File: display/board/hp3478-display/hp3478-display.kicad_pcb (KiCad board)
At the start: 2 copper layers, 130.2 x 29.8 mm, 257 parts, among them J1 SFV10R-1ST, J2 DNP, U1 PIC16F15274-I/MP, U2 DNP

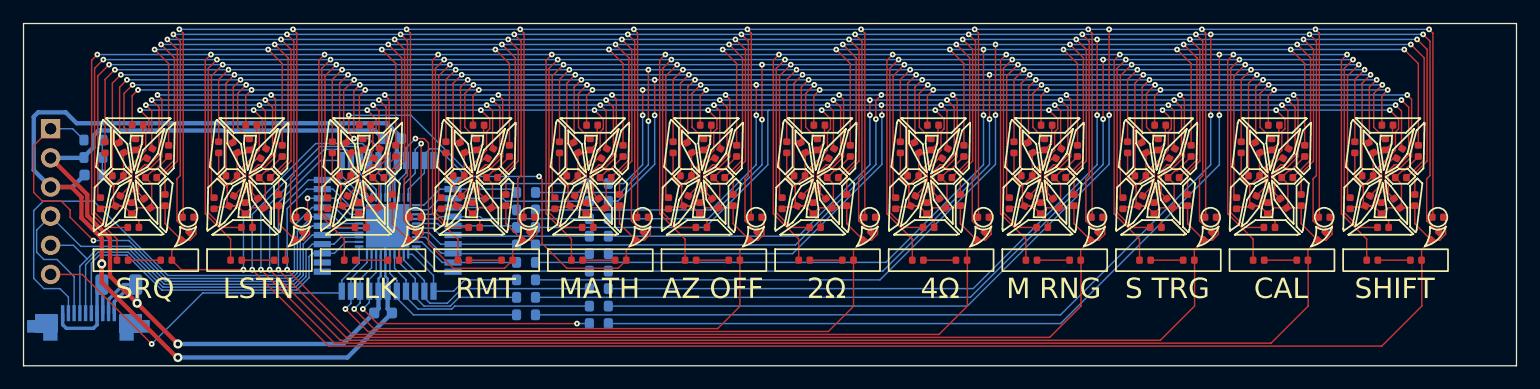
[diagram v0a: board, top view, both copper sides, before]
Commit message: Add mounting holes and fiducials.
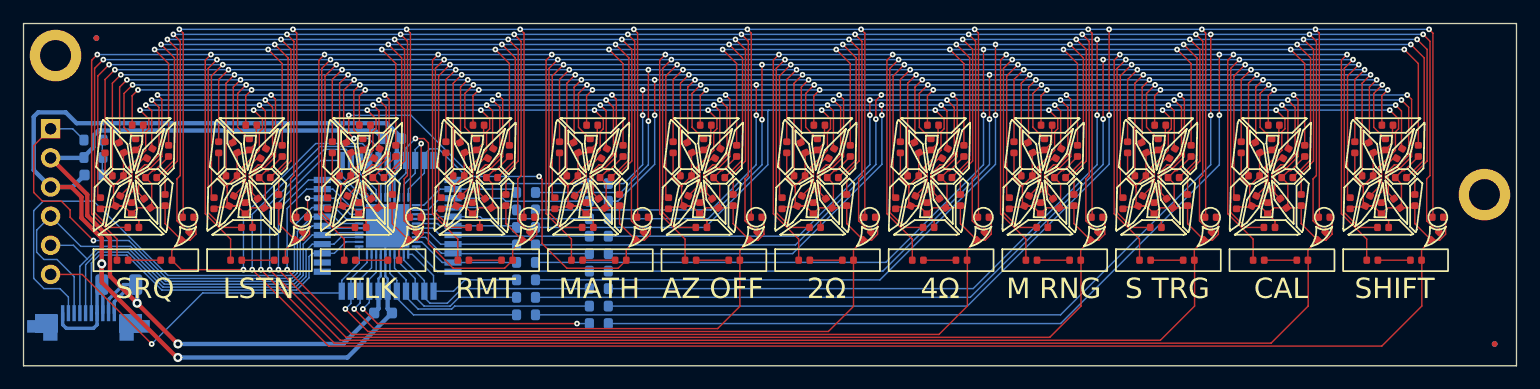
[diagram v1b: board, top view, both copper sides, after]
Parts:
- added FD1: Fiducial_0.5mm_Mask1.5mm, Fiducial:Fiducial_0.5mm_Mask1.5mm, F.Cu at (82.5, 52.1)
- added FD2: Fiducial_0.5mm_Mask1.5mm, Fiducial:Fiducial_0.5mm_Mask1.5mm, F.Cu at (204.5, 78.7)
- added FD3: Fiducial_0.5mm_Mask1.5mm, Fiducial:Fiducial_0.5mm_Mask1.5mm, B.Cu at (82.5, 52.1)
- added FD4: Fiducial_0.5mm_Mask1.5mm, Fiducial:Fiducial_0.5mm_Mask1.5mm, B.Cu at (204.5, 78.7)
- added MH1: MountingHole_2.7mm_M2.5_ISO14580_Pad, MountingHole:MountingHole_2.7mm_M2.5_ISO14580_Pad, F.Cu at (79.0, 53.6)
- added MH2: MountingHole_2.7mm_M2.5_ISO14580_Pad, MountingHole:MountingHole_2.7mm_M2.5_ISO14580_Pad, F.Cu at (203.6, 65.7)
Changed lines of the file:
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@@
     )
   )
+  (footprint "Fiducial:Fiducial_0.5mm_Mask1.5mm" (layer "F.Cu")
+    (at 204.47 78.74)
+    (descr "Circular Fiducial, 0.5mm bare copper, 1.5mm soldermask opening")
+    (tags "fiducial")
+    (attr smd board_only exclude_from_bom)
+    (fp_text reference "FD2" (at 0 -1.7145) (layer "F.SilkS") hide
+      (effects (font (size 1 1) (thickness 0.15)))
+    )
+    (fp_text value "Fiducial_0.5mm_Mask1.5mm" (at 0 1.7145) (layer "F.Fab") hide
+      (effects (font (size 1 1) (thickness 0.15)))
+    )
+    (fp_text user "${REFERENCE}" (at 0 0) (layer "F.Fab") hide
+      (effects (font (size 0.2 0.2) (thickness 0.04)))
+    )
+    (fp_circle (center 0 0) (end 1 0) (layer "F.CrtYd") (width 0.05) (fill none))
+    (fp_circle (center 0 0) (end 0.75 0) (layer "F.Fab") (width 0.1) (fill none))
+    (pad "" smd circle (at 0 0) (size 0.5 0.5) (layers "F.Cu" "F.Mask")
+      (solder_mask_margin 0.5) (clearance 0.5))
+  )
   (footprint "0Local:LED_0402_1005Metric" (layer "F.Cu")
     (at 94.3356 64.0842 180)
@@
     )
   )
+  (footprint "Fiducial:Fiducial_0.5mm_Mask1.5mm" (layer "F.Cu")
+    (at 82.55 52.07)
+    (descr "Circular Fiducial, 0.5mm bare copper, 1.5mm soldermask opening")
+    (tags "fiducial")
+    (attr smd board_only exclude_from_bom)
+    (fp_text reference "FD1" (at 0 -1.7145) (layer "F.SilkS") hide
+      (effects (font (size 1 1) (thickness 0.15)))
+    )
+    (fp_text value "Fiducial_0.5mm_Mask1.5mm" (at 0 1.7145) (layer "F.Fab") hide
+      (effects (font (size 1 1) (thickness 0.15)))
+    )
+    (fp_text user "${REFERENCE}" (at 0 0) (layer "F.Fab") hide
+      (effects (font (size 0.2 0.2) (thickness 0.04)))
+    )
+    (fp_circle (center 0 0) (end 1 0) (layer "F.CrtYd") (width 0.05) (fill none))
+    (fp_circle (center 0 0) (end 0.75 0) (layer "F.Fab") (width 0.1) (fill none))
+    (pad "" smd circle (at 0 0) (size 0.5 0.5) (layers "F.Cu" "F.Mask")
+      (solder_mask_margin 0.5) (clearance 0.5))
+  )
   (footprint "0Local:LED_0402_1005Metric" (layer "F.Cu")
     (at 183.4896 64.0842 180)
@@
     )
   )
+  (footprint "MountingHole:MountingHole_2.7mm_M2.5_ISO14580_Pad" (layer "F.Cu")
+    (at 203.581 65.7225)
+    (descr "Mounting Hole 2.7mm, M2.5, ISO14580")
+    (tags "mounting hole 2.7mm m2.5 iso14580")
+    (attr board_only exclude_from_pos_files exclude_from_bom)
+    (fp_text reference "MH2" (at 0 -3.25) (layer "F.SilkS") hide
+      (effects (font (size 1 1) (thickness 0.15)))
+    )
+    (fp_text value "MountingHole_2.7mm_M2.5_ISO14580_Pad" (at 0 3.25) (layer "F.Fab") hide
+      (effects (font (size 1 1) (thickness 0.15)))
+    )
+    (fp_text user "${REFERENCE}" (at 0 0) (layer "F.Fab") hide
+      (effects (font (size 1 1) (thickness 0.15)))
+    )
+    (fp_circle (center 0 0) (end 2.25 0) (layer "Cmts.User") (width 0.15) (fill none))
+    (fp_circle (center 0 0) (end 2.5 0) (layer "F.CrtYd") (width 0.05) (fill none))
+    (pad "1" thru_hole circle (at 0 0) (size 4.5 4.5) (drill 2.7) (layers *.Cu *.Mask))
+  )
   (footprint "0Local:LED_0402_1005Metric" (layer "F.Cu")
     (at 155.4988 59.6646 180)
@@
     )
   )
+  (footprint "MountingHole:MountingHole_2.7mm_M2.5_ISO14580_Pad" (layer "F.Cu")
+    (at 78.994 53.594)
+    (descr "Mounting Hole 2.7mm, M2.5, ISO14580")
+    (tags "mounting hole 2.7mm m2.5 iso14580")
+    (attr board_only exclude_from_pos_files exclude_from_bom)
+    (fp_text reference "MH1" (at 0 -3.25) (layer "F.SilkS") hide
+      (effects (font (size 1 1) (thickness 0.15)))
+    )
+    (fp_text value "MountingHole_2.7mm_M2.5_ISO14580_Pad" (at 0 3.25) (layer "F.Fab") hide
+      (effects (font (size 1 1) (thickness 0.15)))
+    )
+    (fp_text user "${REFERENCE}" (at 0 0) (layer "F.Fab") hide
+      (effects (font (size 1 1) (thickness 0.15)))
+    )
+    (fp_circle (center 0 0) (end 2.25 0) (layer "Cmts.User") (width 0.15) (fill none))
+    (fp_circle (center 0 0) (end 2.5 0) (layer "F.CrtYd") (width 0.05) (fill none))
+    (pad "1" thru_hole circle (at 0 0) (size 4.5 4.5) (drill 2.7) (layers *.Cu *.Mask))
+  )
   (footprint "0Local:LED_0402_1005Metric" (layer "F.Cu")
     (at 94.3356 66.2686 65)
@@
     )
   )
+  (footprint "Fiducial:Fiducial_0.5mm_Mask1.5mm" (layer "B.Cu")
+    (at 82.55 52.07 180)
+    (descr "Circular Fiducial, 0.5mm bare copper, 1.5mm soldermask opening")
+    (tags "fiducial")
+    (attr smd board_only exclude_from_bom)
+    (fp_text reference "FD3" (at 0 1.7145) (layer "B.SilkS") hide
+      (effects (font (size 1 1) (thickness 0.15)) (justify mirror))
+    )
+    (fp_text value "Fiducial_0.5mm_Mask1.5mm" (at 0 -1.7145) (layer "B.Fab") hide
+      (effects (font (size 1 1) (thickness 0.15)) (justify mirror))
+    )
+    (fp_text user "${REFERENCE}" (at 0 0) (layer "B.Fab") hide
+      (effects (font (size 0.2 0.2) (thickness 0.04)) (justify mirror))
+    )
+    (fp_circle (center 0 0) (end 1 0) (layer "B.CrtYd") (width 0.05) (fill none))
+    (fp_circle (center 0 0) (end 0.75 0) (layer "B.Fab") (width 0.1) (fill none))
+    (pad "" smd circle (at 0 0 180) (size 0.5 0.5) (layers "B.Cu" "B.Mask")
+      (solder_mask_margin 0.5) (clearance 0.5))
+  )
   (footprint "Resistor_SMD:R_0603_1608Metric" (layer "B.Cu")
     (at 120.015 67.056)
@@
     (property "Sheetname" "")
     (attr smd)
-    (fp_text reference "J1" (at -4.191 2.413 unlocked) (layer "B.SilkS")
+    (fp_text reference "J1" (at 3.632 2.573 unlocked) (layer "B.SilkS")
       (effects (font (size 1 1) (thickness 0.15)) (justify mirror))
     )
@@
     )
   )
+  (footprint "Fiducial:Fiducial_0.5mm_Mask1.5mm" (layer "B.Cu")
+    (at 204.47 78.74 180)
+    (descr "Circular Fiducial, 0.5mm bare copper, 1.5mm soldermask opening")
+    (tags "fiducial")
+    (attr smd board_only exclude_from_bom)
+    (fp_text reference "FD4" (at 0 1.7145) (layer "B.SilkS") hide
+      (effects (font (size 1 1) (thickness 0.15)) (justify mirror))
+    )
+    (fp_text value "Fiducial_0.5mm_Mask1.5mm" (at 0 -1.7145) (layer "B.Fab") hide
+      (effects (font (size 1 1) (thickness 0.15)) (justify mirror))
+    )
+    (fp_text user "${REFERENCE}" (at 0 0) (layer "B.Fab") hide
+      (effects (font (size 0.2 0.2) (thickness 0.04)) (justify mirror))
+    )
+    (fp_circle (center 0 0) (end 1 0) (layer "B.CrtYd") (width 0.05) (fill none))
+    (fp_circle (center 0 0) (end 0.75 0) (layer "B.Fab") (width 0.1) (fill none))
+    (pad "" smd circle (at 0 0 180) (size 0.5 0.5) (layers "B.Cu" "B.Mask")
+      (solder_mask_margin 0.5) (clearance 0.5))
+  )
   (footprint "0Local:Symbol_Bonsai_6.7mm" (layer "B.Cu")
     (at 201.58 74.93 180)
@@
     )
   )
-  (gr_rect locked (start 76.2 50.8) (end 206.375 80.645) (layer "Edge.Cuts") (width 0.1) (fill none))
+  (gr_rect (start 76.2 50.8) (end 206.375 80.645) (layer "Edge.Cuts") (width 0.1) (fill none))
   (gr_rect (start 82.296 59.055) (end 200.279 69.215) (layer "User.1") (width 0.15) (fill none))
   (gr_rect (start 82.296 70.485) (end 200.279 72.39) (layer "User.1") (width 0.15) (fill none))

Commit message: Remove MCU and move annunciator LEDs to their own matrix row.
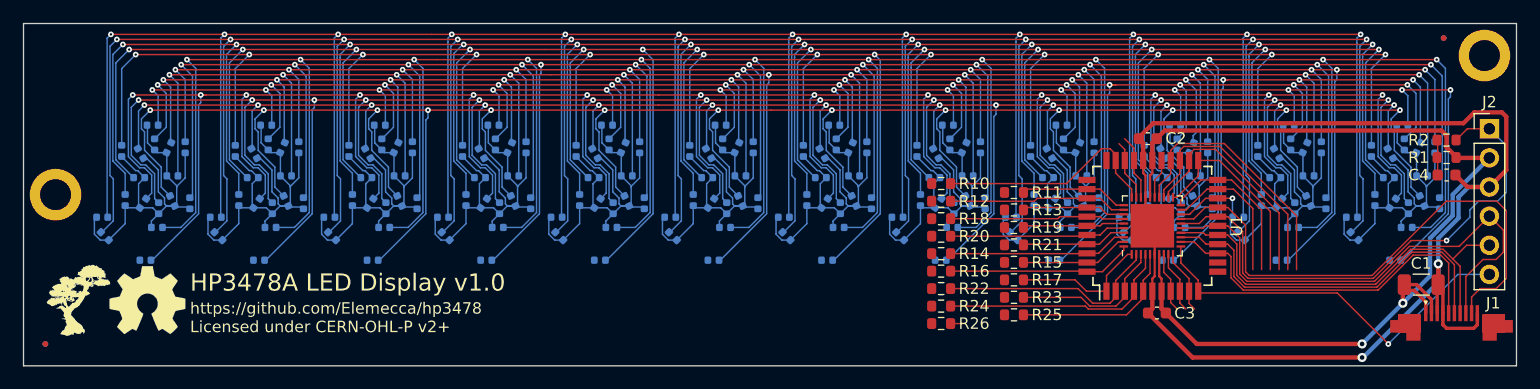
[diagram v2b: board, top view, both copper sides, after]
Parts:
- removed D1018, D1118, D1218, D1318, D218, D318, D418, D518, D618, D718, D818, D918: LED, 0Local:LED_0402_1005Metric
- C1, C2, C3, C4, FD3, FD4, G***, J1, J2, R1, R10, R11, R12, R13, R14, R15, R16, R17, R18, R19, R2, R20, R21, R22, R23, R24, R25, R26, REF**, U1, U2: moved to F.Cu
- D1001, D1002, D1003, D1004, D1005, D1006, D1007, D1008, D1009, D1010, D1011, D1012, D1013, D1014, D1015, D1016, D1101, D1102, D1103, D1104, D1105, D1106, D1107, D1108, D1109, D1110, D1111, D1112, D1113, D1114, D1115, D1116, D1201, D1202, D1203, D1204, D1205, D1206, D1207, D1208, D1209, D1210, D1211, D1212, D1213, D1214, D1215, D1216, D1301, D1302, D1303, D1304, D1305, D1306, D1307, D1308, D1309, D1310, D1311, D1312, D1313, D1314, D1315, D1316, D201, D202, D203, D204, D205, D206, D207, D208, D209, D210, D211, D212, D213, D214, D215, D216, D301, D302, D303, D304, D305, D306, D307, D308, D309, D310, D311, D312, D313, D314, D315, D316, D401, D402, D403, D404, D405, D406, D407, D408, D409, D410, D411, D412, D413, D414, D415, D416, D501, D502, D503, D504, D505, D506, D507, D508, D509, D510, D511, D512, D513, D514, D515, D516, D601, D602, D603, D604, D605, D606, D607, D608, D609, D610, D611, D612, D613, D614, D615, D616, D701, D702, D703, D704, D705, D706, D707, D708, D709, D710, D711, D712, D713, D714, D715, D716, D801, D802, D803, D804, D805, D806, D807, D808, D809, D810, D811, D812, D813, D814, D815, D816, D901, D902, D903, D904, D905, D906, D907, D908, D909, D910, D911, D912, D913, D914, D915, D916, FD1, FD2, MH1, MH2, REF0, REF1, REF10, REF11, REF2, REF3, REF4, REF5, REF6, REF7, REF8, REF9: moved to B.Cu
- D101: renamed from D217; moved to B.Cu
- D102: renamed from D317; moved to B.Cu
- D103: renamed from D417; moved to B.Cu
- D104: renamed from D517; moved to B.Cu
- D105: renamed from D617; moved to B.Cu
- D106: renamed from D717; moved to B.Cu
- D107: renamed from D817; moved to B.Cu
- D108: renamed from D917; moved to B.Cu
- D109: renamed from D1017; moved to B.Cu
- D110: renamed from D1117; moved to B.Cu
- D111: renamed from D1217; moved to B.Cu
- D112: renamed from D1317; moved to B.Cu
- moved FD2 126.4 mm to (78.1, 78.7), turned to 180 degrees
- moved FD4 126.4 mm to (78.1, 78.7), turned to 0 degrees
- moved J2 125.5 mm to (204.0, 60.0), turned to 0 degrees
- moved MH1 124.6 mm to (203.6, 53.6), turned to 180 degrees
- moved MH2 124.6 mm to (79.0, 65.7), turned to 180 degrees
- moved G*** 120.6 mm to (81.0, 74.9), turned to 0 degrees
- moved J1 118.8 mm to (200.7, 77.8), turned to 0 degrees
- moved C4 118.0 mm to (200.3, 64.0), turned to 0 degrees
- moved R1 118.0 mm to (200.3, 62.5), turned to 0 degrees
- moved R2 118.0 mm to (200.3, 61.0), turned to 0 degrees
- moved REF0 118.0 mm to (200.3, 69.2), turned to 180 degrees
- moved FD1 117.5 mm to (200.0, 52.1), turned to 180 degrees
- moved FD3 117.5 mm to (200.0, 52.1), turned to 0 degrees
- moved D209 116.8 mm to (199.7, 66.5)
- moved D1315 116.5 mm to (83.1, 67.7), turned to 0 degrees
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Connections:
- D101 pad 1: Net-(D217-Pad1) -> /K12
- D101 pad 2: /A16 -> /A0
- D102 pad 1: Net-(D317-Pad1) -> /K12
- D102 pad 2: /A16 -> /A1
- D103 pad 1: Net-(D417-Pad1) -> /K12
- D103 pad 2: /A16 -> /A2
- D104 pad 1: Net-(D517-Pad1) -> /K12
- D104 pad 2: /A16 -> /A3
- D105 pad 1: Net-(D617-Pad1) -> /K12
- D105 pad 2: /A16 -> /A4
- D106 pad 1: Net-(D717-Pad1) -> /K12
- D106 pad 2: /A16 -> /A5
- D107 pad 1: Net-(D817-Pad1) -> /K12
- D107 pad 2: /A16 -> /A6
- D108 pad 1: Net-(D917-Pad1) -> /K12
- D108 pad 2: /A16 -> /A7
- D109 pad 1: Net-(D1017-Pad1) -> /K12
- D109 pad 2: /A16 -> /A8
- D110 pad 1: Net-(D1117-Pad1) -> /K12
- D110 pad 2: /A16 -> /A9
- D111 pad 1: Net-(D1217-Pad1) -> /K12
- D111 pad 2: /A16 -> /A10
- D112 pad 1: Net-(D1317-Pad1) -> /K12
- D112 pad 2: /A16 -> /A11
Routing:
- net /A16: track 406.2 -> 0.00 mm, vias 14 -> 0
- net /K11: track 171.7 -> 59.4 mm, vias 1 -> 0
- net /K10: track 159.1 -> 57.6 mm, vias 1 -> 0
- net /K9: track 146.0 -> 55.4 mm, vias 1 -> 0
- net /A15: track 402.1 -> 321.1 mm, vias 14 -> 12
- net /K8: track 132.1 -> 52.4 mm, vias 1 -> 0
- net /K7: track 119.7 -> 50.9 mm, vias 1 -> 0
- net /A14: track 368.1 -> 302.2 mm, vias 14 -> 12
- net /A13: track 377.4 -> 314.0 mm, vias 14 -> 12
- net /A12: track 338.8 -> 275.6 mm, vias 14 -> 12
- net /K6: track 95.6 -> 43.4 mm, vias 1 -> 0
- net /K5: track 84.5 -> 43.3 mm, vias 1 -> 0
- net /K4: track 82.6 -> 41.3 mm, vias 3 -> 0
- net /A7: track 316.5 -> 277.0 mm, vias 14 -> 13
- net /A5: track 267.9 -> 230.0 mm, vias 14 -> 13
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
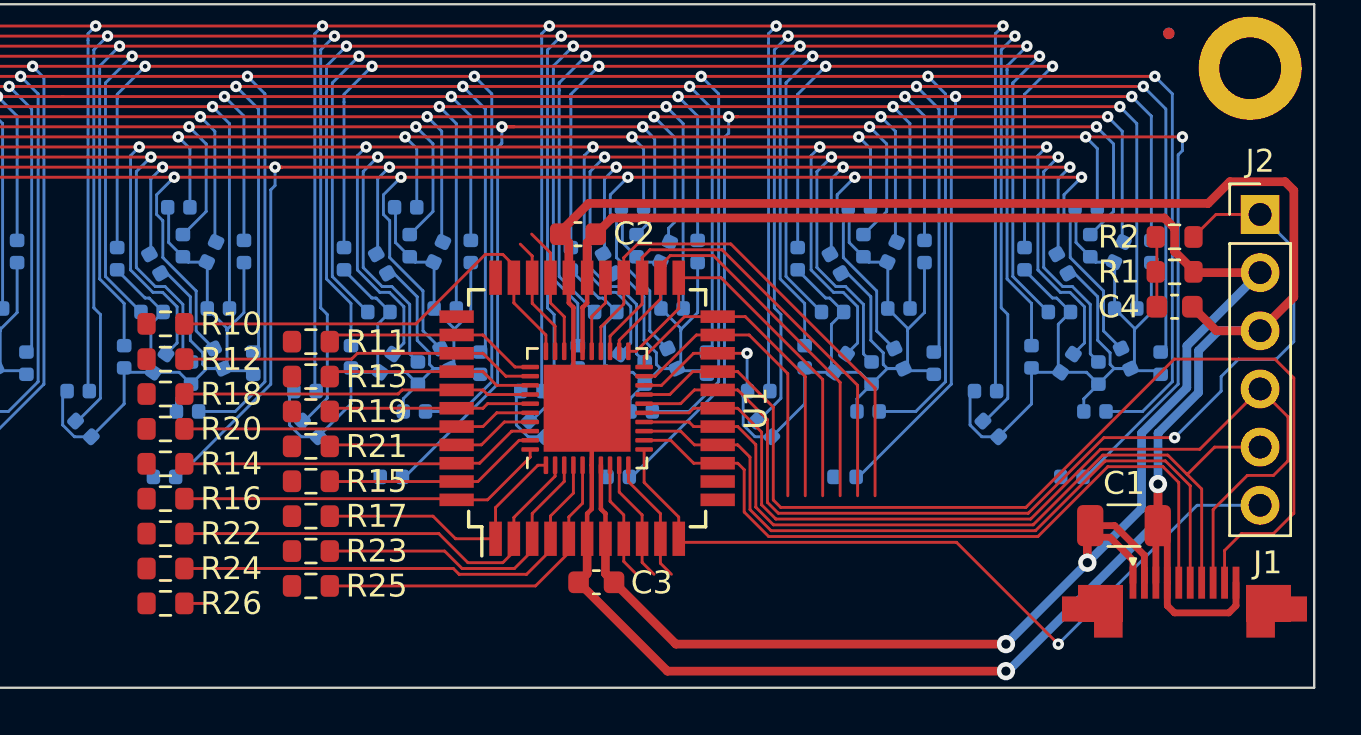
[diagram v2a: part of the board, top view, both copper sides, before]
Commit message: Swap out MCU and add high-side driver.
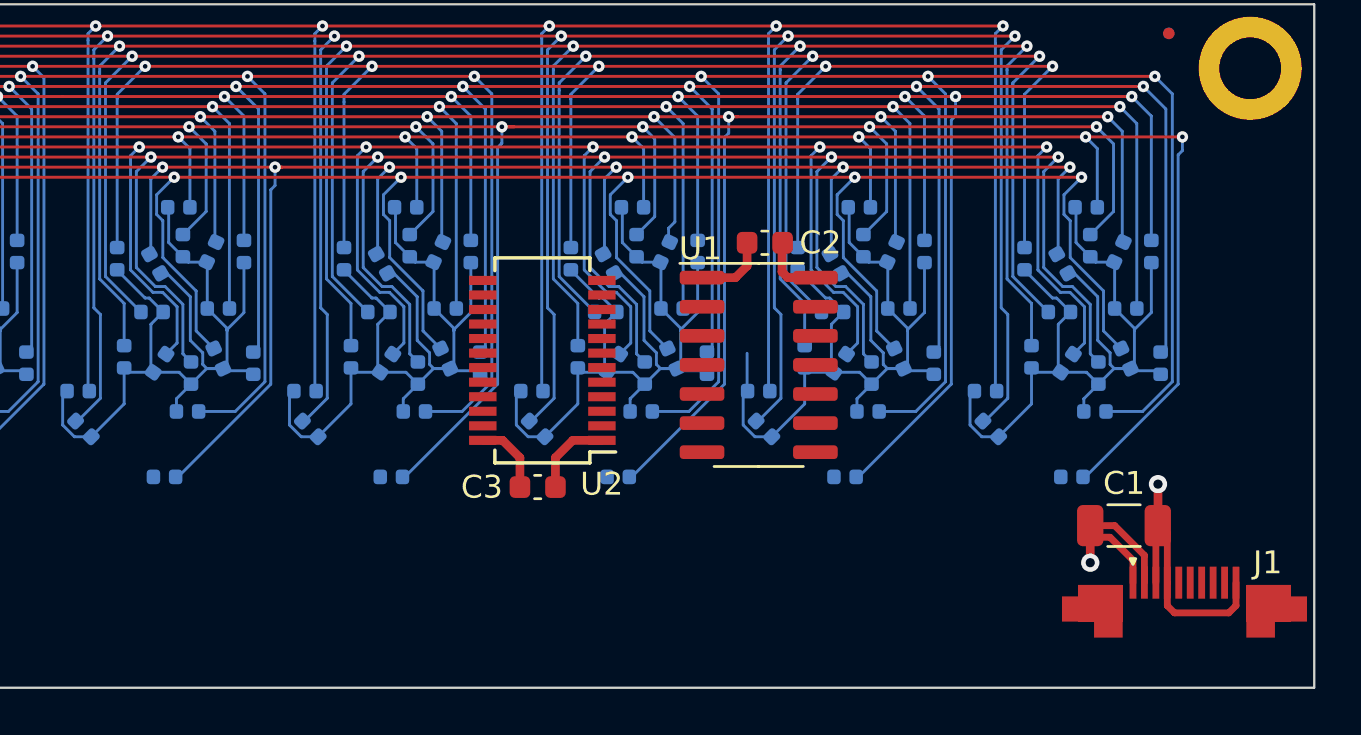
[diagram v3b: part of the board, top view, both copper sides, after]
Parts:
- removed C4: 10n, Capacitor_SMD:C_0603_1608Metric
- removed J2: DNP, Connector_PinHeader_2.54mm:PinHeader_1x06_P2.54mm_Vertical
- removed R1: 10k, Resistor_SMD:R_0603_1608Metric
- removed R10, R11, R12, R13, R14, R15, R16, R17, R18, R19, R20, R21, R22, R23, R24, R25, R26: R, Resistor_SMD:R_0603_1608Metric
- removed R2: 470R, Resistor_SMD:R_0603_1608Metric
- U1: value PIC16F15274-I/MP -> FT60F1x2; footprint Package_DFN_QFN:QFN-40-1EP_5x5mm_P0.4mm_EP3.8x3.8mm -> Package_SO:SO-14_3.9x8.65mm_P1.27mm
- U2: value DNP -> SM16206; footprint Package_QFP:TQFP-44_10x10mm_P0.8mm -> Package_SO:SSOP-24_3.9x8.7mm_P0.635mm
- moved C2 8.17 mm to (182.4, 61.2), turned to 0 degrees
- moved U1 7.73 mm to (182.1, 66.5), turned to 0 degrees
- moved C3 4.88 mm to (172.5, 71.9), turned to 0 degrees
- moved U2 2.86 mm to (172.7, 66.3), turned to 180 degrees
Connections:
- J1 pad 5: /P1 -> /HP1
- J1 pad 6: /SYNC -> /HSYNC
- J1 pad 7: /PGC/ISA -> /HISA
- J1 pad 8: /PGD/IWA -> /HIWA
- J1 pad 9: /PWO -> /HPWO
- U1 pad 1: /HA7 -> +5V
- U1 pad 10: /K6 -> /HPWO
- U1 pad 11: /DBG -> /HP1
- U1 pad 12: /P1 -> /PGD
- U1 pad 13: /SYNC -> /PGC
- U1 pad 14: /PGC/ISA -> GND
- U1 pad 2: /HA12 -> unconnected-(U1-Pad2)
- U1 pad 3: /HA13 -> /HIWA
- U1 pad 4: /HA14 -> /HISA
- U1 pad 5: /HA15 -> /HSYNC
- U1 pad 6: GND -> /DSC
- U1 pad 7: +5V -> /~{DOE}
- U1 pad 8: /HA16 -> /DLC
- U1 pad 9: /K5 -> /DSD
- U2 pad 1: /HA7 -> GND
- U2 pad 10: /K6 -> /A5
- U2 pad 11: /DBG -> /A6
- U2 pad 12: (no net) -> /A7
- U2 pad 13: (no net) -> /A8
- U2 pad 14: /P1 -> /A9
- U2 pad 15: /SYNC -> /A10
- U2 pad 16: /PGC/ISA -> /A11
- U2 pad 17: /PGD/IWA -> /A12
- U2 pad 18: /~{MCLR} -> /A13
- U2 pad 19: /PWO -> /A14
- U2 pad 2: /HA12 -> /DSD
- U2 pad 20: /K1 -> /A15
- U2 pad 21: /K7 -> /~{DOE}
- U2 pad 22: /K8 -> /DSD2
- U2 pad 23: /K9 -> unconnected-(U2-Pad23)
- U2 pad 24: /K10 -> +5V
- U2 pad 3: /HA13 -> /DSC
- U2 pad 4: /HA14 -> /DLC
- U2 pad 5: /HA15 -> /A0
- U2 pad 6: GND -> /A1
- U2 pad 7: +5V -> /A2
- U2 pad 8: /HA16 -> /A3
- U2 pad 9: /K5 -> /A4
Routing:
- net GND: track 110.6 -> 18.7 mm, vias 2 -> 1
- net +5V: track 89.9 -> 15.7 mm, vias 2 -> 1
- net /PWO: track 47.7 -> 0.00 mm
- net /~{MCLR}: track 45.9 -> 0.00 mm, vias 1 -> 0
- net /PGD/IWA: track 44.2 -> 0.00 mm
- net /PGC/ISA: track 37.5 -> 0.00 mm
- net /DBG: track 34.3 -> 0.00 mm, vias 1 -> 0
- net /SYNC: track 32.9 -> 0.00 mm
- net /P1: track 32.1 -> 0.00 mm
- net /K0: track 60.9 -> 37.9 mm
- net /K11: track 59.4 -> 37.9 mm
- net /HA14: track 20.7 -> 0.00 mm
- net /HA0: track 20.2 -> 0.00 mm
- net /K10: track 57.6 -> 37.9 mm
- net /HA12: track 19.6 -> 0.00 mm
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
